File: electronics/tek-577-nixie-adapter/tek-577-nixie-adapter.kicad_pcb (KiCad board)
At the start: 2 copper layers, 76.8 x 61 mm, 6 parts, among them J1 C, J2 Conn_01x11_Socket, J3 E

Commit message: routing improvements
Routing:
- net /C: track 99.9 -> 143.6 mm, vias 2 -> 3
- net /8: track 117.7 -> 120.2 mm
- net /4: track 101.0 -> 100.3 mm
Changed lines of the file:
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@@
     (effects (font (size 2 2) (thickness 0.15)) (justify left bottom))
   )
+  (segment (start 152.4 95.25) (end 153.493357 96.343357) (width 0.25) (layer "F.Cu") (net 1))
+  (segment (start 149.225 88.239915) (end 152.4 91.414915) (width 0.25) (layer "F.Cu") (net 1))
+  (segment (start 196.85 81.28) (end 197.3 81.73) (width 0.25) (layer "F.Cu") (net 1))
+  (segment (start 153.493357 96.343357) (end 154.92327 96.343357) (width 0.25) (layer "F.Cu") (net 1))
+  (segment (start 149.225 81.28) (end 149.225 88.239915) (width 0.25) (layer "F.Cu") (net 1))
+  (segment (start 193.657056 101.98) (end 191.96 101.98) (width 0.25) (layer "F.Cu") (net 1))
+  (segment (start 197.3 98.337056) (end 193.657056 101.98) (width 0.25) (layer "F.Cu") (net 1))
+  (segment (start 197.3 81.73) (end 197.3 98.337056) (width 0.25) (layer "F.Cu") (net 1))
+  (segment (start 152.4 91.414915) (end 152.4 95.25) (width 0.25) (layer "F.Cu") (net 1))
   (via (at 189.865 116.84) (size 0.8) (drill 0.4) (layers "F.Cu" "B.Cu") (net 1))
-  (via (at 147.955 80.645) (size 0.8) (drill 0.4) (layers "F.Cu" "B.Cu") (net 1))
+  (via (at 149.225 81.28) (size 0.8) (drill 0.4) (layers "F.Cu" "B.Cu") (net 1))
+  (via (at 196.85 81.28) (size 0.8) (drill 0.4) (layers "F.Cu" "B.Cu") (net 1))
   (segment (start 191.96 114.745) (end 189.865 116.84) (width 0.25) (layer "B.Cu") (net 1))
+  (segment (start 154.92327 96.343357) (end 154.92327 97.13827) (width 0.25) (layer "B.Cu") (net 1))
+  (segment (start 165.735 93.417085) (end 167.637403 91.514682) (width 0.25) (layer "B.Cu") (net 1))
+  (segment (start 149.225 81.28) (end 148.59 81.28) (width 0.25) (layer "B.Cu") (net 1))
+  (segment (start 162.56 100.33) (end 165.735 97.155) (width 0.25) (layer "B.Cu") (net 1))
+  (segment (start 191.96 101.98) (end 191.96 114.745) (width 0.25) (layer "B.Cu") (net 1))
   (segment (start 154.92327 97.13827) (end 158.115 100.33) (width 0.25) (layer "B.Cu") (net 1))
-  (segment (start 153.778082 89.426918) (end 152.869716 90.335284) (width 0.25) (layer "B.Cu") (net 1))
-  (segment (start 147.955 80.645) (end 153.778082 86.468082) (width 0.25) (layer "B.Cu") (net 1))
-  (segment (start 162.56 100.33) (end 165.959619 96.930381) (width 0.25) (layer "B.Cu") (net 1))
-  (segment (start 169.545 95.816308) (end 169.545 93.422279) (width 0.25) (layer "B.Cu") (net 1))
-  (segment (start 154.92327 96.343357) (end 154.92327 97.13827) (width 0.25) (layer "B.Cu") (net 1))
-  (segment (start 154.128357 96.343357) (end 154.92327 96.343357) (width 0.25) (layer "B.Cu") (net 1))
-  (segment (start 142.24 74.93) (end 147.955 80.645) (width 0.25) (layer "B.Cu") (net 1))
-  (segment (start 169.545 95.816308) (end 184.469646 95.816308) (width 0.25) (layer "B.Cu") (net 1))
+  (segment (start 165.735 97.155) (end 165.735 93.417085) (width 0.25) (layer "B.Cu") (net 1))
   (segment (start 158.115 100.33) (end 162.56 100.33) (width 0.25) (layer "B.Cu") (net 1))
-  (segment (start 169.545 93.422279) (end 167.637403 91.514682) (width 0.25) (layer "B.Cu") (net 1))
-  (segment (start 168.430927 96.930381) (end 169.545 95.816308) (width 0.25) (layer "B.Cu") (net 1))
-  (segment (start 152.869716 95.084716) (end 154.128357 96.343357) (width 0.25) (layer "B.Cu") (net 1))
-  (segment (start 191.96 101.98) (end 191.96 114.745) (width 0.25) (layer "B.Cu") (net 1))
-  (segment (start 134.62 74.93) (end 142.24 74.93) (width 0.25) (layer "B.Cu") (net 1))
-  (segment (start 153.778082 86.468082) (end 153.778082 89.426918) (width 0.25) (layer "B.Cu") (net 1))
-  (segment (start 184.469646 95.816308) (end 190.633338 101.98) (width 0.25) (layer "B.Cu") (net 1))
-  (segment (start 165.959619 96.930381) (end 168.430927 96.930381) (width 0.25) (layer "B.Cu") (net 1))
-  (segment (start 152.869716 90.335284) (end 152.869716 95.084716) (width 0.25) (layer "B.Cu") (net 1))
-  (segment (start 190.633338 101.98) (end 191.96 101.98) (width 0.25) (layer "B.Cu") (net 1))
+  (segment (start 149.225 81.28) (end 196.85 81.28) (width 0.25) (layer "B.Cu") (net 1))
+  (segment (start 148.59 81.28) (end 142.24 74.93) (width 0.25) (layer "B.Cu") (net 1))
+  (segment (start 142.24 74.93) (end 134.62 74.93) (width 0.25) (layer "B.Cu") (net 1))
   (segment (start 135.695 95.055) (end 134.62 93.98) (width 0.25) (layer "F.Cu") (net 2))
   (segment (start 134.62 113.03) (end 135.695 111.955) (width 0.25) (layer "F.Cu") (net 2))
@@
   (segment (start 177.8 93.89) (end 182.21 89.48) (width 0.25) (layer "F.Cu") (net 6))
   (segment (start 164.567362 96.930381) (end 164.567362 94.749303) (width 0.25) (layer "F.Cu") (net 6))
-  (segment (start 163.83 108.585) (end 163.83 107.86) (width 0.25) (layer "F.Cu") (net 6))
   (segment (start 159.385 113.03) (end 163.83 108.585) (width 0.25) (layer "F.Cu") (net 6))
   (segment (start 143.51 100.33) (end 138.519331 95.339331) (width 0.25) (layer "F.Cu") (net 6))
@@
   (segment (start 159.39156 89.218657) (end 159.036716 89.218657) (width 0.25) (layer "B.Cu") (net 9))
   (segment (start 193.71 83.855) (end 193.71 89.48) (width 0.25) (layer "F.Cu") (net 10))
+  (segment (start 156.845 81.28) (end 153.035 77.47) (width 0.25) (layer "F.Cu") (net 10))
   (segment (start 187.325 77.47) (end 193.71 83.855) (width 0.25) (layer "F.Cu") (net 10))
   (segment (start 129.645669 88.792935) (end 129.645669 94.171969) (width 0.25) (layer "F.Cu") (net 10))
@@
   (segment (start 153.035 77.47) (end 140.968604 77.47) (width 0.25) (layer "F.Cu") (net 10))
   (segment (start 140.968604 77.47) (end 129.645669 88.792935) (width 0.25) (layer "F.Cu") (net 10))
-  (segment (start 156.845 81.28) (end 156.845 83.82) (width 0.25) (layer "F.Cu") (net 10))
-  (segment (start 153.035 77.47) (end 156.845 81.28) (width 0.25) (layer "F.Cu") (net 10))
+  (segment (start 156.845 83.185) (end 156.845 81.28) (width 0.25) (layer "F.Cu") (net 10))
   (via (at 187.325 77.47) (size 0.8) (drill 0.4) (layers "F.Cu" "B.Cu") (net 10))
   (via (at 153.035 77.47) (size 0.8) (drill 0.4) (layers "F.Cu" "B.Cu") (net 10))
-  (via (at 156.845 83.82) (size 0.8) (drill 0.4) (layers "F.Cu" "B.Cu") (net 10))
-  (segment (start 162.608478 83.574807) (end 164.268606 85.234935) (width 0.25) (layer "B.Cu") (net 10))
-  (segment (start 164.268606 85.234935) (end 164.268606 90.608606) (width 0.25) (layer "B.Cu") (net 10))
-  (segment (start 164.268606 90.608606) (end 167.914616 94.254616) (width 0.25) (layer "B.Cu") (net 10))
-  (segment (start 156.845 83.82) (end 156.845 89.671827) (width 0.25) (layer "B.Cu") (net 10))
-  (segment (start 167.914616 94.254616) (end 167.914616 95.290016) (width 0.25) (layer "B.Cu") (net 10))
+  (via (at 156.845 83.185) (size 0.8) (drill 0.4) (layers "F.Cu" "B.Cu") (net 10))
+  (segment (start 156.845 83.185) (end 164.465 83.185) (width 0.25) (layer "B.Cu") (net 10))
+  (segment (start 156.845 83.185) (end 156.845 89.671827) (width 0.25) (layer "B.Cu") (net 10))
   (segment (start 156.845 89.671827) (end 156.661816 89.855011) (width 0.25) (layer "B.Cu") (net 10))
+  (segment (start 164.465 83.185) (end 169.162403 87.882403) (width 0.25) (layer "B.Cu") (net 10))
   (segment (start 153.035 77.47) (end 187.325 77.47) (width 0.25) (layer "B.Cu") (net 10))
-  (segment (start 156.845 83.82) (end 157.090193 83.574807) (width 0.25) (layer "B.Cu") (net 10))
-  (segment (start 157.090193 83.574807) (end 162.608478 83.574807) (width 0.25) (layer "B.Cu") (net 10))
+  (segment (start 169.162403 87.882403) (end 169.162403 94.042229) (width 0.25) (layer "B.Cu") (net 10))
+  (segment (start 169.162403 94.042229) (end 167.914616 95.290016) (width 0.25) (layer "B.Cu") (net 10))
   (segment (start 131.266338 88.9) (end 130.720669 89.445669) (width 0.25) (layer "F.Cu") (net 11))
   (segment (start 151.765 78.74) (end 141.605 78.74) (width 0.25) (layer "F.Cu") (net 11))

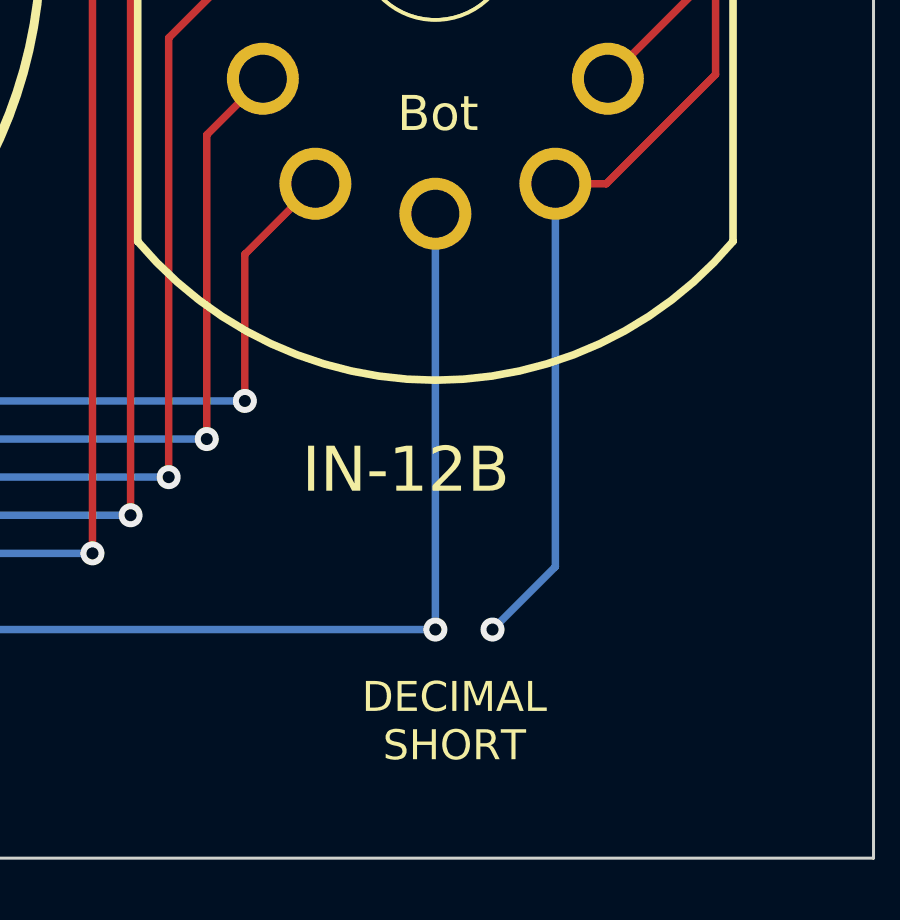
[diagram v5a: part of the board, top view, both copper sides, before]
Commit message: fixing decimal point short with jumper
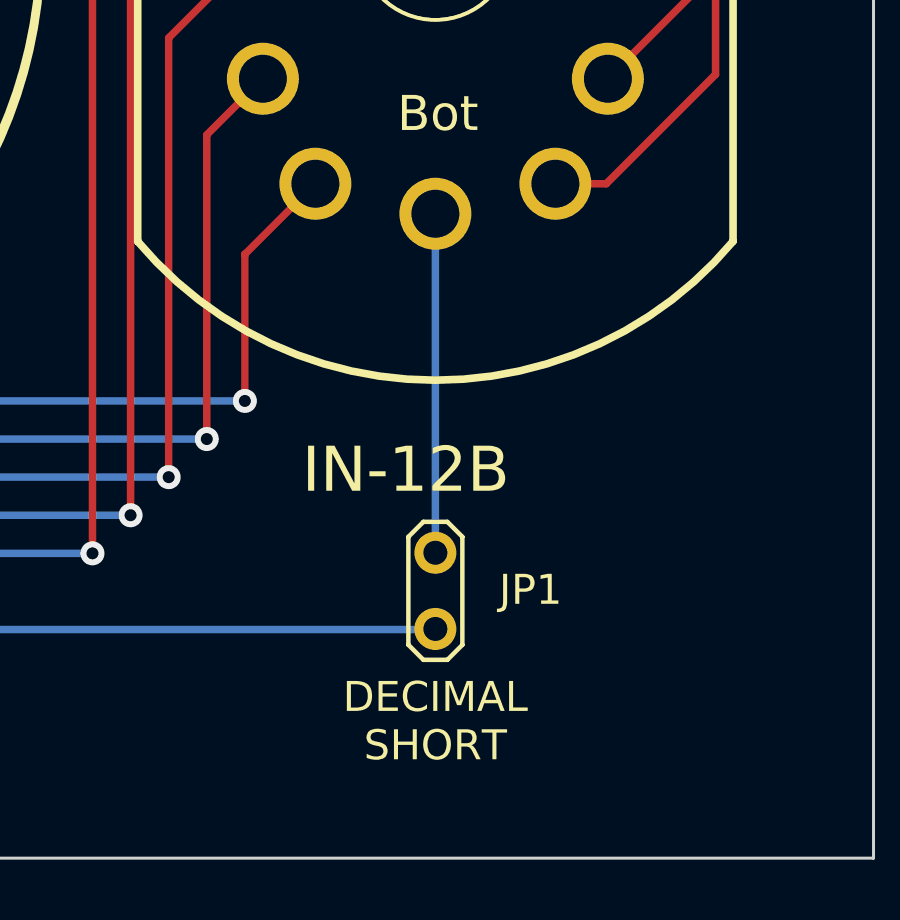
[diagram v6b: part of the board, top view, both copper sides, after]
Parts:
- added JP1: DecimalPoint, TestPoint:TestPoint_2Pads_Pitch2.54mm_Drill0.8mm, F.Cu at (188.0, 116.8)
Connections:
- NX1 pad LHDP: /E -> Net-(JP1-B)
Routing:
- net /C: track 143.6 -> 127.9 mm, vias 3 -> 2
- net /E: track 88.7 -> 74.9 mm, vias 1 -> 0
- net Net-(JP1-B): track 0.00 -> 11.3 mm
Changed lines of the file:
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@@
   (net 11 "/9")
   (net 12 "/0")
+  (net 13 "Net-(JP1-B)")
   (footprint "MountingHole:MountingHole_4mm_Pad_TopBottom" (layer "F.Cu")
     (at 134.62 74.93)
@@
     (pad "A" thru_hole circle (at -4.113446 2.3749 210) (size 2.1844 2.1844) (drill 1.6) (layers "*.Cu" "*.Mask")
       (net 1 "/C") (pinfunction "A") (pintype "bidirectional") (solder_mask_margin 0.1016))
+  )
+  (footprint "TestPoint:TestPoint_2Pads_Pitch2.54mm_Drill0.8mm" (layer "F.Cu")
+    (at 187.96 116.82 90)
+    (descr "Test point with 2 pins, pitch 2.54mm, drill diameter 0.8mm")
+    (tags "CONN DEV")
+    (property "Sheetfile" "tek-577-nixie-adapter.kicad_sch")
+    (property "Sheetname" "")
+    (property "ki_description" "Jumper, 2-pole, open")
+    (property "ki_keywords" "Jumper SPST")
+    (attr exclude_from_pos_files)
+    (fp_text reference "JP1" (at 1.3 3.175 180) (layer "F.SilkS")
+        (effects (font (size 1 1) (thickness 0.15)))
+    )
+    (fp_text value "DecimalPoint" (at 1.27 2 90) (layer "F.Fab")
+        (effects (font (size 1 1) (thickness 0.15)))
+    )
+    (fp_text user "${REFERENCE}" (at 1.3 -2 90) (layer "F.Fab")
+        (effects (font (size 1 1) (thickness 0.15)))
+    )
+    (fp_line (start -1.03 -0.4) (end -0.53 -0.9)
+      (stroke (width 0.15) (type solid)) (layer "F.SilkS"))
+    (fp_line (start -1.03 0.4) (end -1.03 -0.4)
+      (stroke (width 0.15) (type solid)) (layer "F.SilkS"))
+    (fp_line (start -0.53 -0.9) (end 3.07 -0.9)
+      (stroke (width 0.15) (type solid)) (layer "F.SilkS"))
+    (fp_line (start -0.53 0.9) (end -1.03 0.4)
+      (stroke (width 0.15) (type solid)) (layer "F.SilkS"))
+    (fp_line (start 3.07 -0.9) (end 3.57 -0.4)
+      (stroke (width 0.15) (type solid)) (layer "F.SilkS"))
+    (fp_line (start 3.07 0.9) (end -0.53 0.9)
+      (stroke (width 0.15) (type solid)) (layer "F.SilkS"))
+    (fp_line (start 3.57 -0.4) (end 3.57 0.4)
+      (stroke (width 0.15) (type solid)) (layer "F.SilkS"))
+    (fp_line (start 3.57 0.4) (end 3.07 0.9)
+      (stroke (width 0.15) (type solid)) (layer "F.SilkS"))
+    (fp_line (start -1.3 -0.5) (end -1.3 0.5)
+      (stroke (width 0.05) (type solid)) (layer "F.CrtYd"))
+    (fp_line (start -1.3 0.5) (end -0.65 1.15)
+      (stroke (width 0.05) (type solid)) (layer "F.CrtYd"))
+    (fp_line (start -0.65 -1.15) (end -1.3 -0.5)
+      (stroke (width 0.05) (type solid)) (layer "F.CrtYd"))
+    (fp_line (start -0.65 1.15) (end 3.15 1.15)
+      (stroke (width 0.05) (type solid)) (layer "F.CrtYd"))
+    (fp_line (start 3.15 -1.15) (end -0.65 -1.15)
+      (stroke (width 0.05) (type solid)) (layer "F.CrtYd"))
+    (fp_line (start 3.15 1.15) (end 3.8 0.5)
+      (stroke (width 0.05) (type solid)) (layer "F.CrtYd"))
+    (fp_line (start 3.8 -0.5) (end 3.15 -1.15)
+      (stroke (width 0.05) (type solid)) (layer "F.CrtYd"))
+    (fp_line (start 3.8 0.5) (end 3.8 -0.5)
+      (stroke (width 0.05) (type solid)) (layer "F.CrtYd"))
+    (pad "1" thru_hole circle (at 0 0 90) (size 1.4 1.4) (drill 0.8) (layers "*.Cu" "*.Mask")
+      (net 2 "/E") (pinfunction "A") (pintype "passive"))
+    (pad "2" thru_hole circle (at 2.54 0 90) (size 1.4 1.4) (drill 0.8) (layers "*.Cu" "*.Mask")
+      (net 13 "Net-(JP1-B)") (pinfunction "B") (pintype "passive"))
   )
   (footprint "nixie-us:IN-4-DSUB" (layer "F.Cu")
@@
       (net 1 "/C") (pinfunction "A") (pintype "bidirectional") (solder_mask_margin 0.1016))
     (pad "LHDP" thru_hole circle (at 0 9) (size 2.4 2.4) (drill 1.6) (layers "*.Cu" "*.Mask")
-      (net 2 "/E") (pinfunction "LHDP") (pintype "bidirectional") (solder_mask_margin 0.1016))
+      (net 13 "Net-(JP1-B)") (pinfunction "LHDP") (pintype "bidirectional") (solder_mask_margin 0.1016))
   )
   (footprint "MountingHole:MountingHole_4mm_Pad_TopBottom" (layer "F.Cu")
@@
     (effects (font (size 2 2) (thickness 0.15)) (justify left bottom))
   )
-  (gr_text "DECIMAL\nSHORT" (at 188.595 121.285) (layer "F.SilkS")
+  (gr_text "DECIMAL\nSHORT" (at 187.96 121.285) (layer "F.SilkS")
     (effects (font (size 1 1) (thickness 0.15)) (justify bottom))
   )
@@
   (segment (start 197.3 81.73) (end 197.3 98.337056) (width 0.25) (layer "F.Cu") (net 1))
   (segment (start 152.4 91.414915) (end 152.4 95.25) (width 0.25) (layer "F.Cu") (net 1))
-  (via (at 189.865 116.84) (size 0.8) (drill 0.4) (layers "F.Cu" "B.Cu") (net 1))
   (via (at 149.225 81.28) (size 0.8) (drill 0.4) (layers "F.Cu" "B.Cu") (net 1))
   (via (at 196.85 81.28) (size 0.8) (drill 0.4) (layers "F.Cu" "B.Cu") (net 1))
-  (segment (start 191.96 114.745) (end 189.865 116.84) (width 0.25) (layer "B.Cu") (net 1))
   (segment (start 154.92327 96.343357) (end 154.92327 97.13827) (width 0.25) (layer "B.Cu") (net 1))
   (segment (start 165.735 93.417085) (end 167.637403 91.514682) (width 0.25) (layer "B.Cu") (net 1))
   (segment (start 149.225 81.28) (end 148.59 81.28) (width 0.25) (layer "B.Cu") (net 1))
   (segment (start 162.56 100.33) (end 165.735 97.155) (width 0.25) (layer "B.Cu") (net 1))
-  (segment (start 191.96 101.98) (end 191.96 114.745) (width 0.25) (layer "B.Cu") (net 1))
   (segment (start 154.92327 97.13827) (end 158.115 100.33) (width 0.25) (layer "B.Cu") (net 1))
   (segment (start 165.735 97.155) (end 165.735 93.417085) (width 0.25) (layer "B.Cu") (net 1))
@@
   (segment (start 134.62 113.03) (end 135.695 111.955) (width 0.25) (layer "F.Cu") (net 2))
   (segment (start 135.695 111.955) (end 135.695 95.055) (width 0.25) (layer "F.Cu") (net 2))
-  (via (at 187.96 116.84) (size 0.8) (drill 0.4) (layers "F.Cu" "B.Cu") (net 2))
   (segment (start 138.43 116.84) (end 134.62 113.03) (width 0.25) (layer "B.Cu") (net 2))
   (segment (start 187.96 116.84) (end 138.43 116.84) (width 0.25) (layer "B.Cu") (net 2))
-  (segment (start 187.96 102.98) (end 187.96 116.84) (width 0.25) (layer "B.Cu") (net 2))
   (segment (start 145.415 105.41) (end 145.415 95.885) (width 0.25) (layer "F.Cu") (net 3))
   (segment (start 149.225 109.22) (end 145.415 105.41) (width 0.25) (layer "F.Cu") (net 3))
@@
   (via (at 193.675 80.01) (size 0.8) (drill 0.4) (layers "F.Cu" "B.Cu") (net 12))
   (segment (start 193.675 80.01) (end 150.495 80.01) (width 0.25) (layer "B.Cu") (net 12))
+  (segment (start 187.96 102.98) (end 187.96 114.28) (width 0.25) (layer "B.Cu") (net 13))
 )
